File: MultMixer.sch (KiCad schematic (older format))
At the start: 5 parts

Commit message: mult section
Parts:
- added D?: LED, symbol Device:LED
- added J?: Mult IN, symbol Connector:Conn_01x02_Male
- added J?: Out 1, symbol Connector:Conn_01x02_Male
- added J?: Out 2, symbol Connector:Conn_01x02_Male
- added J?: Out 3, symbol Connector:Conn_01x02_Male
- added J?: Out 4, symbol Connector:Conn_01x02_Male
- added J?: Out 5, symbol Connector:Conn_01x02_Male
- added R? (x5): 100r, symbol Device:R
- added R?: 1k, symbol Device:R
- added R?: 10M, symbol Device:R
- added U? (x5): TL074, symbol Amplifier_Operational:TL074
- added U? (x3): TL072, symbol Amplifier_Operational:TL072
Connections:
- net GND: now also D?.1 (K), J?.2 (Pin_2), J?.2 (Pin_2), J?.2 (Pin_2), J?.2 (Pin_2), J?.2 (Pin_2), J?.2 (Pin_2), R?.2
- new net: R?.2, U?.1, U?.2 (-) (x2)
- new net: J?.1 (Pin_1), R?.1, U?.10 (+), U?.12 (+), U?.3 (+), U?.3 (+), U?.5 (+), U?.5 (+)
- new net: R?.2, U?.6 (-), U?.7 (x2)
- new net: R?.2, U?.8, U?.9 (-)
- new net: R?.2, U?.13 (-), U?.14
- new net: J?.1 (Pin_1), R?.1 (x5)
- new net: D?.2 (A), R?.1

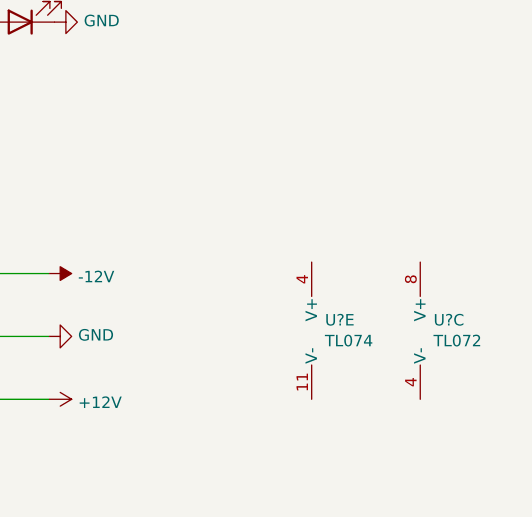
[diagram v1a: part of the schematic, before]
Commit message: op amp power
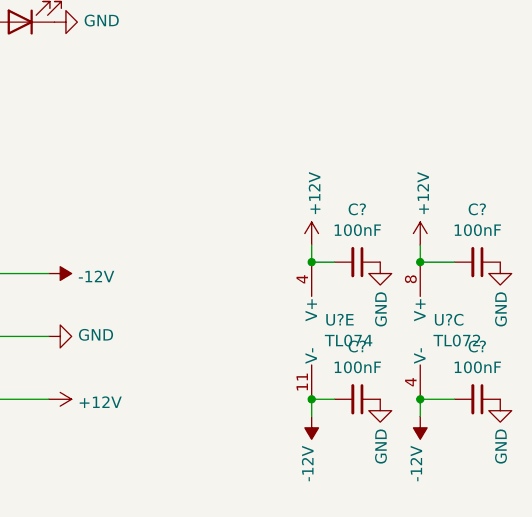
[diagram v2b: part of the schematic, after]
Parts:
- added C? (x4): 100nF, symbol Device:C_Small
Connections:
- net +12V: now also U?.4 (V+), U?.8 (V+), C?.2, C?.2
- net -12V: now also U?.11 (V-), U?.4 (V-), C?.2, C?.2
- net GND: now also C?.1, C?.1, C?.1, C?.1
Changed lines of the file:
@@
 	0    -1   -1   0
 $EndComp
+$Comp
+L power:-12V #PWR?
+U 1 1 60E00578
+P 4650 7200
+F 0 "#PWR?" H 4650 7300 50  0001 C CNN
+F 1 "-12V" V 4665 7328 50  0000 L CNN
+F 2 "" H 4650 7200 50  0001 C CNN
+F 3 "" H 4650 7200 50  0001 C CNN
+	1    4650 7200
+	-1   0    0    1
+$EndComp
+$Comp
+L power:-12V #PWR?
+U 1 1 60E00BF9
+P 5125 7200
+F 0 "#PWR?" H 5125 7300 50  0001 C CNN
+F 1 "-12V" V 5140 7328 50  0000 L CNN
+F 2 "" H 5125 7200 50  0001 C CNN
+F 3 "" H 5125 7200 50  0001 C CNN
+	1    5125 7200
+	-1   0    0    1
+$EndComp
+$Comp
+L power:+12V #PWR?
+U 1 1 60E00EB8
+P 4650 6450
+F 0 "#PWR?" H 4650 6300 50  0001 C CNN
+F 1 "+12V" V 4665 6578 50  0000 L CNN
+F 2 "" H 4650 6450 50  0001 C CNN
+F 3 "" H 4650 6450 50  0001 C CNN
+	1    4650 6450
+	1    0    0    -1
+$EndComp
+$Comp
+L power:+12V #PWR?
+U 1 1 60E01558
+P 5125 6450
+F 0 "#PWR?" H 5125 6300 50  0001 C CNN
+F 1 "+12V" V 5140 6578 50  0000 L CNN
+F 2 "" H 5125 6450 50  0001 C CNN
+F 3 "" H 5125 6450 50  0001 C CNN
+	1    5125 6450
+	1    0    0    -1
+$EndComp
+$Comp
+L Device:C_Small C?
+U 1 1 60E01E25
+P 5375 6525
+F 0 "C?" V 5146 6525 50  0000 C CNN
+F 1 "100nF" V 5237 6525 50  0000 C CNN
+F 2 "" H 5375 6525 50  0001 C CNN
+F 3 "~" H 5375 6525 50  0001 C CNN
+	1    5375 6525
+	0    1    1    0
+$EndComp
+$Comp
+L Device:C_Small C?
+U 1 1 60E02956
+P 5375 7125
+F 0 "C?" V 5146 7125 50  0000 C CNN
+F 1 "100nF" V 5237 7125 50  0000 C CNN
+F 2 "" H 5375 7125 50  0001 C CNN
+F 3 "~" H 5375 7125 50  0001 C CNN
+	1    5375 7125
+	0    1    1    0
+$EndComp
+$Comp
+L Device:C_Small C?
+U 1 1 60E02E5D
+P 4850 7125
+F 0 "C?" V 4621 7125 50  0000 C CNN
+F 1 "100nF" V 4712 7125 50  0000 C CNN
+F 2 "" H 4850 7125 50  0001 C CNN
+F 3 "~" H 4850 7125 50  0001 C CNN
+	1    4850 7125
+	0    1    1    0
+$EndComp
+$Comp
+L Device:C_Small C?
+U 1 1 60E032B1
+P 4850 6525
+F 0 "C?" V 4621 6525 50  0000 C CNN
+F 1 "100nF" V 4712 6525 50  0000 C CNN
+F 2 "" H 4850 6525 50  0001 C CNN
+F 3 "~" H 4850 6525 50  0001 C CNN
+	1    4850 6525
+	0    1    1    0
+$EndComp
+Wire Wire Line
+	4750 6525 4650 6525
+Wire Wire Line
+	4750 7125 4650 7125
+Wire Wire Line
+	5275 7125 5125 7125
+Wire Wire Line
+	5275 6525 5125 6525
+Wire Wire Line
+	5125 6450 5125 6525
+Connection ~ 5125 6525
+Wire Wire Line
+	4650 6450 4650 6525
+Connection ~ 4650 6525
+Wire Wire Line
+	4650 7200 4650 7125
+Connection ~ 4650 7125
+Wire Wire Line
+	5125 7200 5125 7125
+Connection ~ 5125 7125
+$Comp
+L power:GND #PWR?
+U 1 1 60E0DD8C
+P 4950 6525
+F 0 "#PWR?" H 4950 6275 50  0001 C CNN
+F 1 "GND" V 4955 6397 50  0000 R CNN
+F 2 "" H 4950 6525 50  0001 C CNN
+F 3 "" H 4950 6525 50  0001 C CNN
+	1    4950 6525
+	1    0    0    -1
+$EndComp
+$Comp
+L power:GND #PWR?
+U 1 1 60E0E43F
+P 4950 7125
+F 0 "#PWR?" H 4950 6875 50  0001 C CNN
+F 1 "GND" V 4955 6997 50  0000 R CNN
+F 2 "" H 4950 7125 50  0001 C CNN
+F 3 "" H 4950 7125 50  0001 C CNN
+	1    4950 7125
+	1    0    0    -1
+$EndComp
+$Comp
+L power:GND #PWR?
+U 1 1 60E0E7A2
+P 5475 7125
+F 0 "#PWR?" H 5475 6875 50  0001 C CNN
+F 1 "GND" V 5480 6997 50  0000 R CNN
+F 2 "" H 5475 7125 50  0001 C CNN
+F 3 "" H 5475 7125 50  0001 C CNN
+	1    5475 7125
+	1    0    0    -1
+$EndComp
+$Comp
+L power:GND #PWR?
+U 1 1 60E0E9C7
+P 5475 6525
+F 0 "#PWR?" H 5475 6275 50  0001 C CNN
+F 1 "GND" V 5480 6397 50  0000 R CNN
+F 2 "" H 5475 6525 50  0001 C CNN
+F 3 "" H 5475 6525 50  0001 C CNN
+	1    5475 6525
+	1    0    0    -1
+$EndComp
 $EndSCHEMATC

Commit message: start mixer section
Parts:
- added R?: 100k, symbol Device:R
- added RV?: 100k, symbol Device:R_POT
- added SW?: on/off, symbol Switch:SW_SPDT
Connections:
- net GND: now also RV?.3
- new net: RV?.1, SW?.1 (A)
- new net: R?.1, RV?.2
- no-connect marks 0 -> 1
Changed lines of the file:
@@
 	1    0    0    -1
 $EndComp
+$Comp
+L Switch:SW_SPDT SW?
+U 1 1 60E108C2
+P 6050 1475
+F 0 "SW?" H 6050 1760 50  0000 C CNN
+F 1 "on/off" H 6050 1669 50  0000 C CNN
+F 2 "" H 6050 1475 50  0001 C CNN
+F 3 "~" H 6050 1475 50  0001 C CNN
+	1    6050 1475
+	1    0    0    -1
+$EndComp
+$Comp
+L Device:R_POT RV?
+U 1 1 60E10F19
+P 6425 1525
+F 0 "RV?" H 6550 1775 50  0000 R CNN
+F 1 "100k" H 6650 1700 50  0000 R CNN
+F 2 "" H 6425 1525 50  0001 C CNN
+F 3 "~" H 6425 1525 50  0001 C CNN
+	1    6425 1525
+	1    0    0    -1
+$EndComp
+NoConn ~ 6250 1575
+$Comp
+L power:GND #PWR?
+U 1 1 60E1407A
+P 6425 1675
+F 0 "#PWR?" H 6425 1425 50  0001 C CNN
+F 1 "GND" H 6430 1502 50  0000 C CNN
+F 2 "" H 6425 1675 50  0001 C CNN
+F 3 "" H 6425 1675 50  0001 C CNN
+	1    6425 1675
+	-1   0    0    -1
+$EndComp
+Wire Wire Line
+	6250 1375 6425 1375
+$Comp
+L Device:R R?
+U 1 1 60E16553
+P 6725 1525
+F 0 "R?" V 6900 1475 50  0000 C CNN
+F 1 "100k" V 6825 1475 50  0000 C CNN
+F 2 "" V 6655 1525 50  0001 C CNN
+F 3 "~" H 6725 1525 50  0001 C CNN
+	1    6725 1525
+	0    -1   -1   0
+$EndComp
 $EndSCHEMATC

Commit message: mixer section
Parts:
- removed U? (x2): TL072, symbol Amplifier_Operational:TL072
- added C? (x2): 100pF, symbol Device:C
- added J?: In 1, symbol Connector:Conn_01x02_Male
- added J?: In 2, symbol Connector:Conn_01x02_Male
- added J?: In 3, symbol Connector:Conn_01x02_Male
- added J?: In 4, symbol Connector:Conn_01x02_Male
- added J?: In 5, symbol Connector:Conn_01x02_Male
- added R? (x7): 100k, symbol Device:R
- added RV? (x4): 100k, symbol Device:R_POT
- added SW? (x4): on/off, symbol Switch:SW_SPDT
- added U? (x4): TL074, symbol Amplifier_Operational:TL074
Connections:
- net GND: now also J?.2 (Pin_2), J?.2 (Pin_2), J?.2 (Pin_2), J?.2 (Pin_2), J?.2 (Pin_2), RV?.3, RV?.3, RV?.3, RV?.3, U?.10 (+), U?.12 (+)
- net at J?.1 (Pin_1), R?.1, U?.10 (+)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: now also U?.3 (+), U?.5 (+)
- net at R?.2: now also U?.1, U?.2 (-)
- net at R?.2: now also U?.6 (-), U?.7
- net at SW?.2 (B): now also J?.1 (Pin_1)
- net at R?.2: now also C?.2, R?.1, R?.2, R?.2, R?.2, R?.2, U?.9 (-)
- new net: RV?.1, SW?.1 (A) (x4)
- new net: J?.1 (Pin_1), SW?.2 (B) (x4)
- new net: R?.1, RV?.2 (x4)
- new net: C?.1, R?.1, R?.2, U?.8
- new net: C?.2, R?.1, R?.2, U?.13 (-)
- new net: C?.1, R?.2, U?.14
- no-connect marks 1 -> 5
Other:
- moved on the sheet: R?, RV?, SW?

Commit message: mixer power
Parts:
- removed U?: TL072, symbol Amplifier_Operational:TL072
- added U?: TL074, symbol Amplifier_Operational:TL074
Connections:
- net +12V: now also U?.4 (V+)
- net -12V: now also U?.11 (V-)
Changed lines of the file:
@@
-$EndComp
-$Comp
-L Amplifier_Operational:TL072 U?
-U 3 1 60DD91E3
-P 5225 6825
-F 0 "U?" H 5183 6871 50  0000 L CNN
-F 1 "TL072" H 5183 6780 50  0000 L CNN
-F 2 "" H 5225 6825 50  0001 C CNN
-F 3 "http://www.ti.com/lit/ds/symlink/tl071.pdf" H 5225 6825 50  0001 C CNN
-	3    5225 6825
-	1    0    0    -1
 $EndComp
 $Comp
@@
 Wire Wire Line
 	5125 6450 5125 6525
-Connection ~ 5125 6525
 Wire Wire Line
 	4650 6450 4650 6525
@@
 Wire Wire Line
 	5125 7200 5125 7125
-Connection ~ 5125 7125
 $Comp
 L power:GND #PWR?
@@
 Wire Wire Line
 	9200 3025 9250 3025
+$Comp
+L Amplifier_Operational:TL074 U?
+U 5 1 60E1517D
+P 5225 6825
+F 0 "U?" H 5183 6871 50  0000 L CNN
+F 1 "TL074" H 5183 6780 50  0000 L CNN
+F 2 "" H 5175 6925 50  0001 C CNN
+F 3 "http://www.ti.com/lit/ds/symlink/tl071.pdf" H 5275 7025 50  0001 C CNN
+	5    5225 6825
+	1    0    0    -1
+$EndComp
+Connection ~ 5125 7125
+Connection ~ 5125 6525
 $EndSCHEMATC

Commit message: annotate and finish schem!
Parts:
- C3, C4, C5, C6, C7, C8: renamed from C?; footprint (none) -> Sonosus:Capacitor_NonPolarized
- D3: renamed from D?; footprint (none) -> LED_THT:LED_D5.0mm
- J1, J10, J11, J12, J3, J4, J5, J6, J7, J8, J9: renamed from J?; footprint (none) -> Connector_PinHeader_2.54mm:PinHeader_1x02_P2.54mm_Vertical
- R1, R10, R11, R12, R13, R14, R15, R2, R3, R4, R5, R6, R7, R8, R9: renamed from R?; footprint (none) -> Sonosus:Resistor
- RV1, RV2, RV3, RV4, RV5: renamed from RV?; footprint (none) -> Sonosus:Potentiometer_Alpha_RD901F-40-00D_centred
- SW1, SW2, SW3, SW4, SW5: renamed from SW?; footprint (none) -> My_Components:SPST_Toggle_A-3643
- U1, U2: renamed from U?; footprint (none) -> Sonosus:DIP-14_Socket
- gave numbers to parts that had none: 5

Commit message: output jack
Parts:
- added J?: In 2, Connector_PinHeader_2.54mm:PinHeader_1x02_P2.54mm_Vertical, symbol Connector:Conn_01x02_Male
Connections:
- net GND: now also J?.2 (Pin_2)
- net at C8.1, R15.2, U2.14: now also J?.1 (Pin_1)
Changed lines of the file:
@@
 Wire Wire Line
 	3425 6850 3500 6850
+$Comp
+L Connector:Conn_01x02_Male J?
+U 1 1 60DE3CCC
+P 10075 2925
+F 0 "J?" H 10183 3106 50  0000 C CNN
+F 1 "In 2" H 10183 3015 50  0000 C CNN
+F 2 "Connector_PinHeader_2.54mm:PinHeader_1x02_P2.54mm_Vertical" H 10075 2925 50  0001 C CNN
+F 3 "~" H 10075 2925 50  0001 C CNN
+	1    10075 2925
+	-1   0    0    -1
+$EndComp
+Wire Wire Line
+	9875 2925 9800 2925
+Connection ~ 9800 2925
+$Comp
+L power:GND #PWR?
+U 1 1 60DE9AA5
+P 9875 3025
+F 0 "#PWR?" H 9875 2775 50  0001 C CNN
+F 1 "GND" H 9880 2852 50  0000 C CNN
+F 2 "" H 9875 3025 50  0001 C CNN
+F 3 "" H 9875 3025 50  0001 C CNN
+	1    9875 3025
+	-1   0    0    -1
+$EndComp
 $EndSCHEMATC

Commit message: back annotate
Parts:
- J1, J10, J11, J12, J3, J4, J5, J6, J7, J8, J9, J?: footprint Connector_PinHeader_2.54mm:PinHeader_1x02_P2.54mm_Vertical -> Connector_Molex:Molex_KK-254_AE-6410-02A_1x02_P2.54mm_Vertical
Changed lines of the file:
@@
 F 0 "J1" H 1458 1456 50  0000 C CNN
 F 1 "Mult IN" H 1458 1365 50  0000 C CNN
-F 2 "Connector_PinHeader_2.54mm:PinHeader_1x02_P2.54mm_Vertical" H 1350 1275 50  0001 C CNN
+F 2 "Connector_Molex:Molex_KK-254_AE-6410-02A_1x02_P2.54mm_Vertical" H 1350 1275 50  0001 C CNN
 F 3 "~" H 1350 1275 50  0001 C CNN
 	1    1350 1275
@@
 F 0 "J3" H 3372 1449 50  0000 R CNN
 F 1 "Out 1" H 3372 1358 50  0000 R CNN
-F 2 "Connector_PinHeader_2.54mm:PinHeader_1x02_P2.54mm_Vertical" H 3400 1475 50  0001 C CNN
+F 2 "Connector_Molex:Molex_KK-254_AE-6410-02A_1x02_P2.54mm_Vertical" H 3400 1475 50  0001 C CNN
 F 3 "~" H 3400 1475 50  0001 C CNN
 	1    3400 1475
@@
 F 0 "J4" H 3372 2274 50  0000 R CNN
 F 1 "Out 2" H 3372 2183 50  0000 R CNN
-F 2 "Connector_PinHeader_2.54mm:PinHeader_1x02_P2.54mm_Vertical" H 3400 2300 50  0001 C CNN
+F 2 "Connector_Molex:Molex_KK-254_AE-6410-02A_1x02_P2.54mm_Vertical" H 3400 2300 50  0001 C CNN
 F 3 "~" H 3400 2300 50  0001 C CNN
 	1    3400 2300
@@
 F 0 "J6" H 3397 3174 50  0000 R CNN
 F 1 "Out 3" H 3397 3083 50  0000 R CNN
-F 2 "Connector_PinHeader_2.54mm:PinHeader_1x02_P2.54mm_Vertical" H 3425 3200 50  0001 C CNN
+F 2 "Connector_Molex:Molex_KK-254_AE-6410-02A_1x02_P2.54mm_Vertical" H 3425 3200 50  0001 C CNN
 F 3 "~" H 3425 3200 50  0001 C CNN
 	1    3425 3200
@@
 F 0 "J5" H 3508 4206 50  0000 C CNN
 F 1 "Out 4" H 3325 4125 50  0000 C CNN
-F 2 "Connector_PinHeader_2.54mm:PinHeader_1x02_P2.54mm_Vertical" H 3400 4025 50  0001 C CNN
+F 2 "Connector_Molex:Molex_KK-254_AE-6410-02A_1x02_P2.54mm_Vertical" H 3400 4025 50  0001 C CNN
 F 3 "~" H 3400 4025 50  0001 C CNN
 	1    3400 4025
@@
 F 0 "J7" H 3533 4956 50  0000 C CNN
 F 1 "Out 5" H 3325 4875 50  0000 C CNN
-F 2 "Connector_PinHeader_2.54mm:PinHeader_1x02_P2.54mm_Vertical" H 3425 4775 50  0001 C CNN
+F 2 "Connector_Molex:Molex_KK-254_AE-6410-02A_1x02_P2.54mm_Vertical" H 3425 4775 50  0001 C CNN
 F 3 "~" H 3425 4775 50  0001 C CNN
 	1    3425 4775
@@
 F 0 "J8" H 5858 1631 50  0000 C CNN
 F 1 "In 1" H 5858 1540 50  0000 C CNN
-F 2 "Connector_PinHeader_2.54mm:PinHeader_1x02_P2.54mm_Vertical" H 5750 1450 50  0001 C CNN
+F 2 "Connector_Molex:Molex_KK-254_AE-6410-02A_1x02_P2.54mm_Vertical" H 5750 1450 50  0001 C CNN
 F 3 "~" H 5750 1450 50  0001 C CNN
 	1    5750 1450
@@
 F 0 "J9" H 5858 2431 50  0000 C CNN
 F 1 "In 2" H 5858 2340 50  0000 C CNN
-F 2 "Connector_PinHeader_2.54mm:PinHeader_1x02_P2.54mm_Vertical" H 5750 2250 50  0001 C CNN
+F 2 "Connector_Molex:Molex_KK-254_AE-6410-02A_1x02_P2.54mm_Vertical" H 5750 2250 50  0001 C CNN
 F 3 "~" H 5750 2250 50  0001 C CNN
 	1    5750 2250
@@
 F 0 "J10" H 5858 3181 50  0000 C CNN
 F 1 "In 3" H 5858 3090 50  0000 C CNN
-F 2 "Connector_PinHeader_2.54mm:PinHeader_1x02_P2.54mm_Vertical" H 5750 3000 50  0001 C CNN
+F 2 "Connector_Molex:Molex_KK-254_AE-6410-02A_1x02_P2.54mm_Vertical" H 5750 3000 50  0001 C CNN
 F 3 "~" H 5750 3000 50  0001 C CNN
 	1    5750 3000
@@
 F 0 "J11" H 5858 3981 50  0000 C CNN
 F 1 "In 4" H 5858 3890 50  0000 C CNN
-F 2 "Connector_PinHeader_2.54mm:PinHeader_1x02_P2.54mm_Vertical" H 5750 3800 50  0001 C CNN
+F 2 "Connector_Molex:Molex_KK-254_AE-6410-02A_1x02_P2.54mm_Vertical" H 5750 3800 50  0001 C CNN
 F 3 "~" H 5750 3800 50  0001 C CNN
 	1    5750 3800
@@
 F 0 "J12" H 5858 4706 50  0000 C CNN
 F 1 "In 5" H 5858 4615 50  0000 C CNN
-F 2 "Connector_PinHeader_2.54mm:PinHeader_1x02_P2.54mm_Vertical" H 5750 4525 50  0001 C CNN
+F 2 "Connector_Molex:Molex_KK-254_AE-6410-02A_1x02_P2.54mm_Vertical" H 5750 4525 50  0001 C CNN
 F 3 "~" H 5750 4525 50  0001 C CNN
 	1    5750 4525
@@
 F 0 "J?" H 10183 3106 50  0000 C CNN
 F 1 "In 2" H 10183 3015 50  0000 C CNN
-F 2 "Connector_PinHeader_2.54mm:PinHeader_1x02_P2.54mm_Vertical" H 10075 2925 50  0001 C CNN
+F 2 "Connector_Molex:Molex_KK-254_AE-6410-02A_1x02_P2.54mm_Vertical" H 10075 2925 50  0001 C CNN
 F 3 "~" H 10075 2925 50  0001 C CNN
 	1    10075 2925
@@
 Connection ~ 9800 2925
 $Comp
-L power:GND #PWR?
+L power:GND #PWR0101
 U 1 1 60DE9AA5
 P 9875 3025
-F 0 "#PWR?" H 9875 2775 50  0001 C CNN
+F 0 "#PWR0101" H 9875 2775 50  0001 C CNN
 F 1 "GND" H 9880 2852 50  0000 C CNN
 F 2 "" H 9875 3025 50  0001 C CNN
